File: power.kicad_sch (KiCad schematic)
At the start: 53 parts, among them J25 Conn_01x02, U1 TLV75733PDBV, U2 TPS56A37, U6 TPS5430DDA, U7 TPS56A37

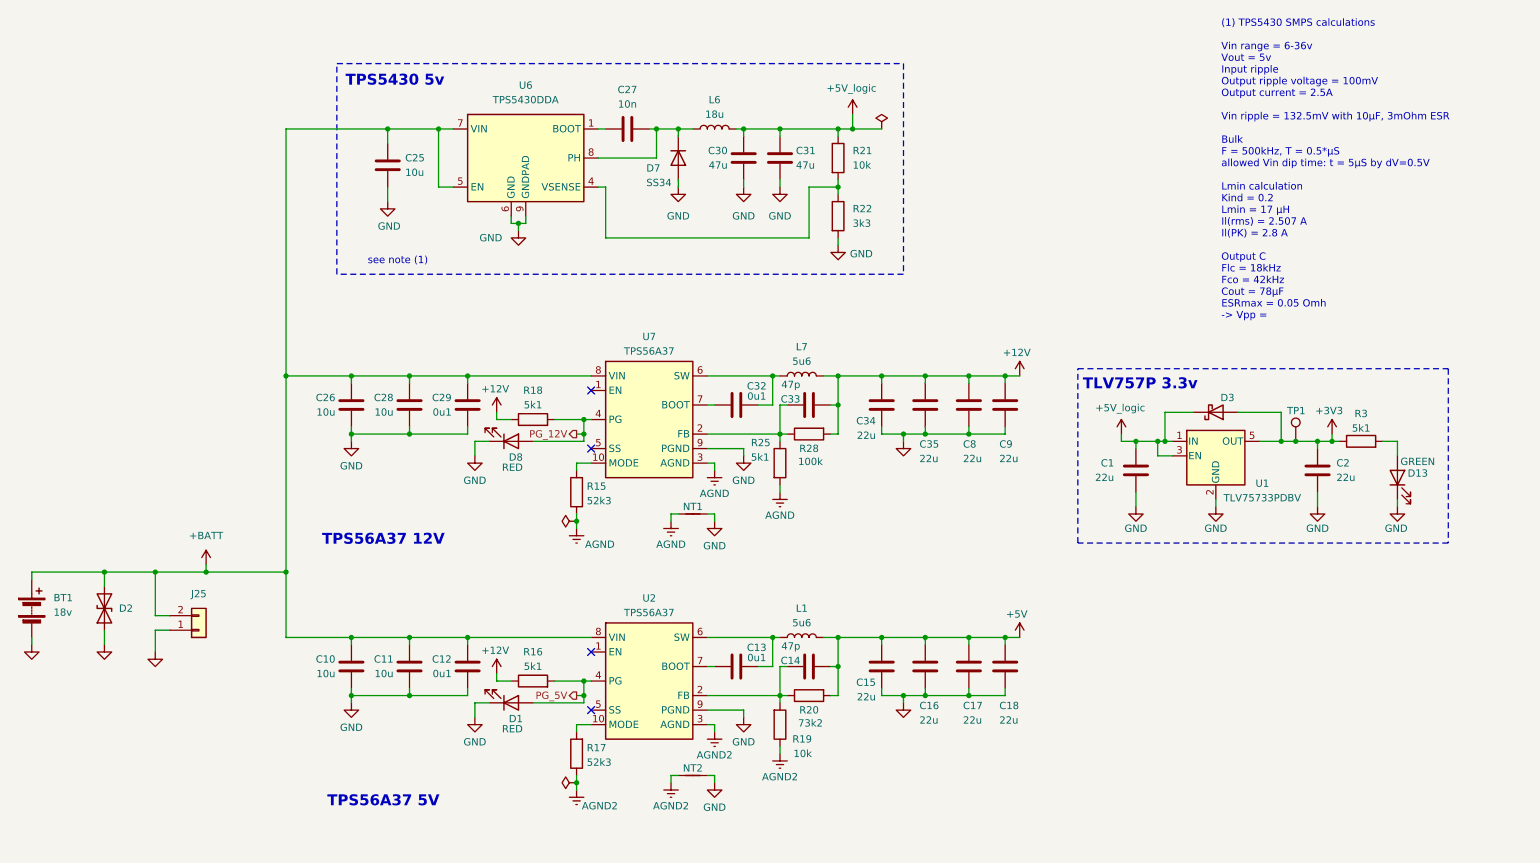
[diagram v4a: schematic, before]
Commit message: schem: remove logic 5V smps
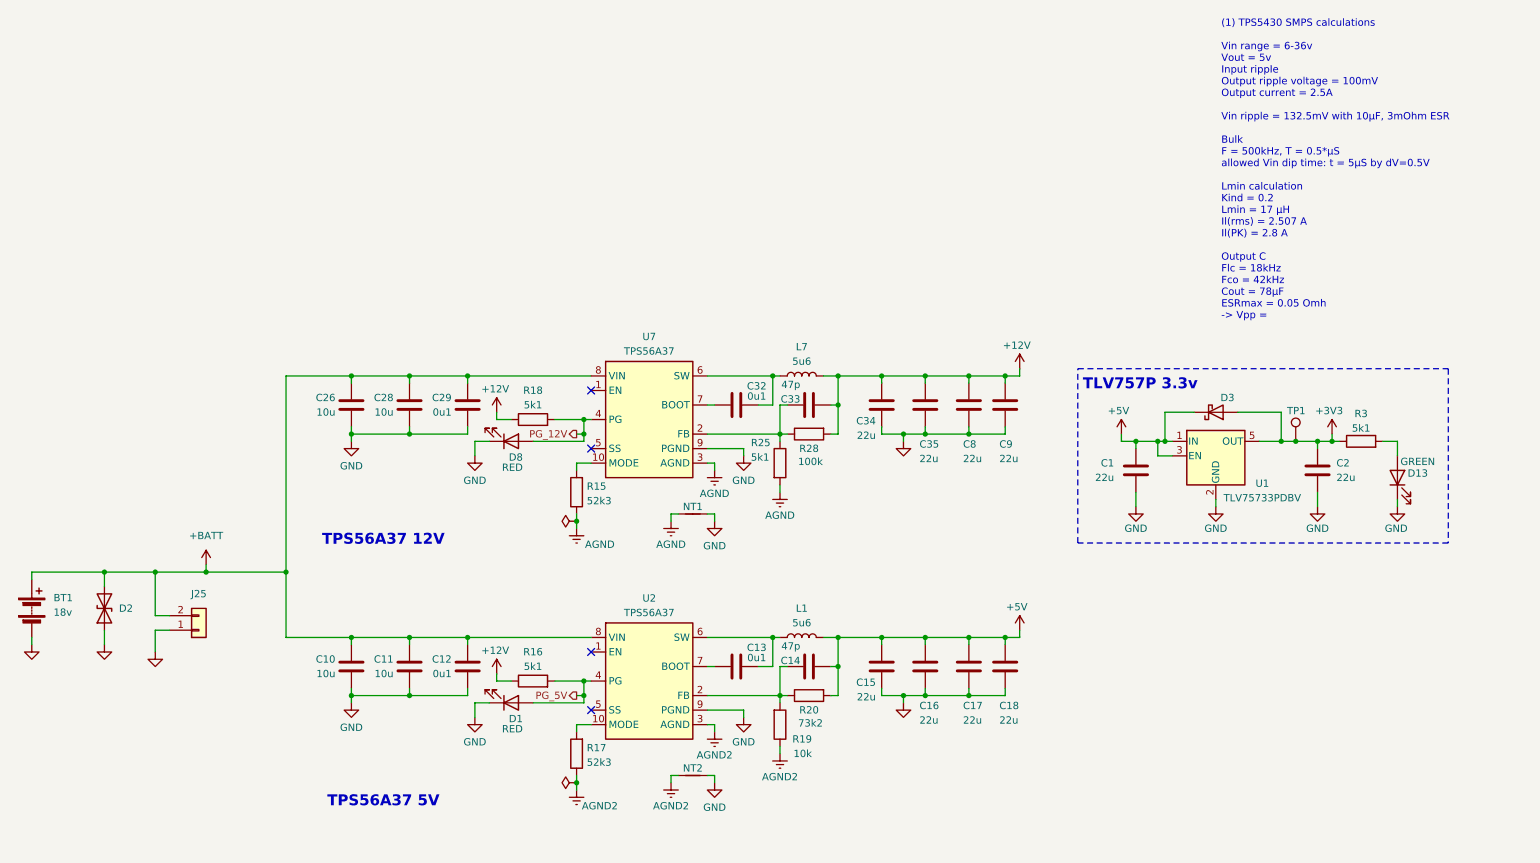
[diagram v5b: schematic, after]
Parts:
- removed C25: 10u, Capacitor_SMD:C_0805_2012Metric, symbol Device:C
- removed C27: 10n, Capacitor_SMD:C_0402_1005Metric, symbol Device:C
- removed C30, C31: 47u, Capacitor_SMD:C_1206_3216Metric, symbol Device:C
- removed D7: SS34, Diode_SMD:D_SMA, symbol Device:D
- removed L6: 18u, Inductor_SMD:L_Sunlord_SWRB1207S, symbol Device:L
- removed R21: 10k, Resistor_SMD:R_0402_1005Metric, symbol Device:R
- removed R22: 3k3, Resistor_SMD:R_0402_1005Metric, symbol Device:R
- removed U6: TPS5430DDA, Package_SO:TI_SO-PowerPAD-8_ThermalVias, symbol Regulator_Switching:TPS5430DDA
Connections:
- net +5V_logic is gone; now on net +5V: C1.2, D3.1 (K), U1.1 (IN), U1.3 (EN)
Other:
- note removed: "TPS5430 5v"
- note removed: "see note (1)"

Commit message: schem: add disable jumper to efuses
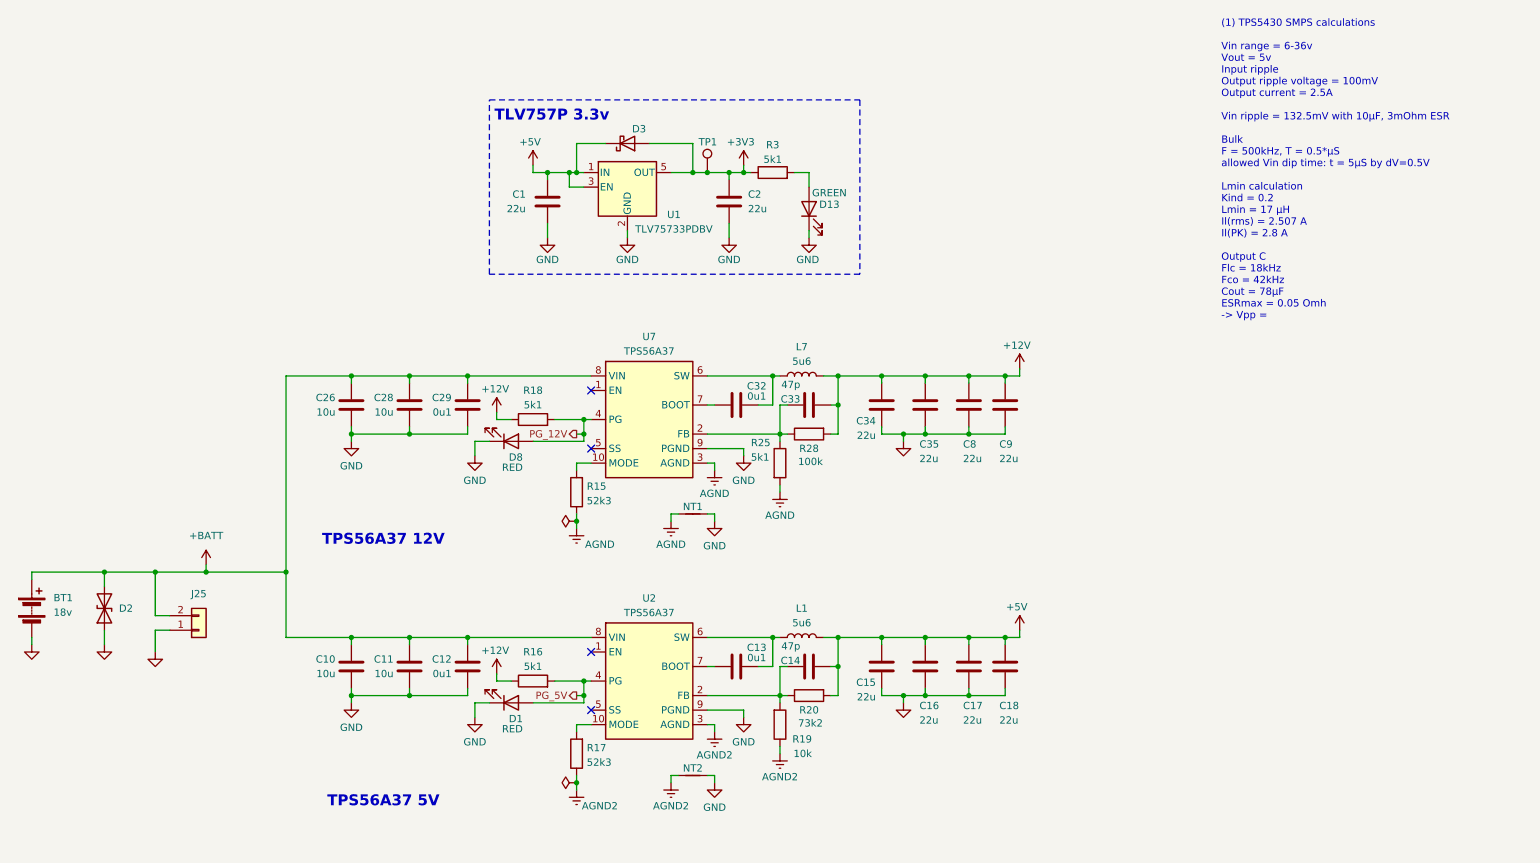
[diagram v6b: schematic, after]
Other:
- moved on the sheet: C1, C2, D13, D3, R3, TP1, U1

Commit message: schem: change aux batt power connector
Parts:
- J25: footprint Connector_JST:JST_XH_B2B-XH-A_1x02_P2.50mm_Vertical -> TerminalBlock_Phoenix:TerminalBlock_Phoenix_MKDS-1,5-2-5.08_1x02_P5.08mm_Horizontal
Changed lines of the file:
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@@
 			)
 		)
-		(property "Footprint" "Connector_JST:JST_XH_B2B-XH-A_1x02_P2.50mm_Vertical"
+		(property "Footprint" "TerminalBlock_Phoenix:TerminalBlock_Phoenix_MKDS-1,5-2-5.08_1x02_P5.08mm_Horizontal"
 			(at 55.88 121.92 0)
 			(effects

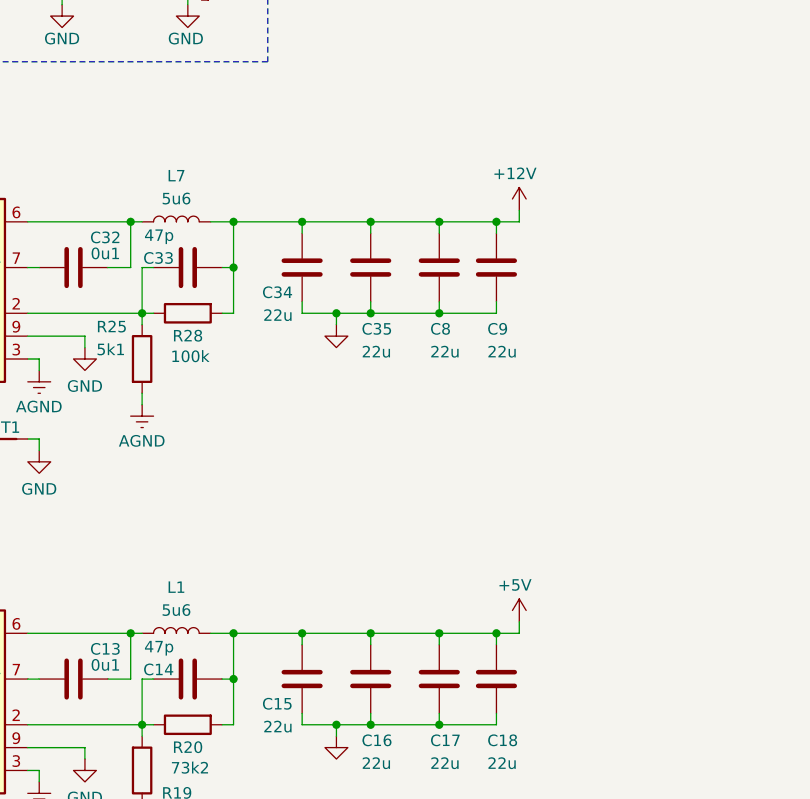
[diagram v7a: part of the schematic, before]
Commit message: schem: add test points
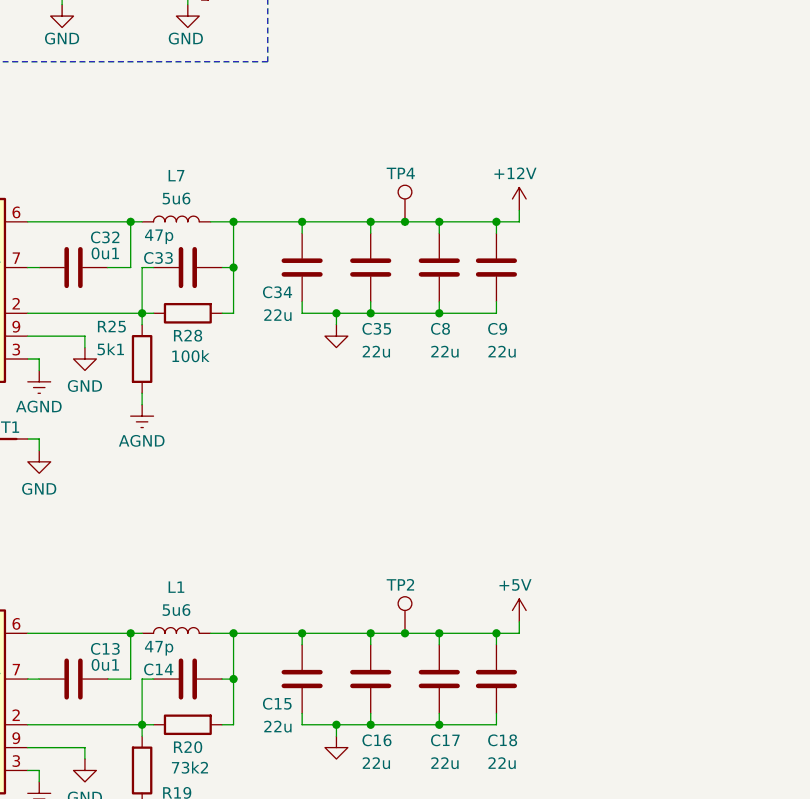
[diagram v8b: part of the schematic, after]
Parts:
- added TP2, TP4: TestPoint, TestPoint:TestPoint_Pad_D2.0mm, symbol Connector:TestPoint
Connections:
- net +12V: now also TP4.1
- net +5V: now also TP2.1
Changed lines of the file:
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@@
 	)
 	(junction
+		(at 186.69 123.19)
+		(diameter 0)
+		(color 0 0 0 0)
+	)
+	(junction
 		(at 167.64 77.47)
 		(diameter 0)
@@
 	)
 	(junction
+		(at 186.69 77.47)
+		(diameter 0)
+		(color 0 0 0 0)
+	)
+	(junction
 		(at 82.55 77.47)
 		(diameter 0)
@@
 	(wire
 		(pts
-			(xy 182.88 123.19) (xy 190.5 123.19)
+			(xy 182.88 123.19) (xy 186.69 123.19)
 		)
 		(stroke
@@
 	(wire
 		(pts
-			(xy 182.88 77.47) (xy 190.5 77.47)
+			(xy 182.88 77.47) (xy 186.69 77.47)
 		)
 		(stroke
@@
 	(wire
 		(pts
+			(xy 186.69 123.19) (xy 190.5 123.19)
+		)
+		(stroke
+			(width 0)
+			(type default)
+		)
+	)
+	(wire
+		(pts
 			(xy 138.43 101.6) (xy 139.7 101.6)
 		)
@@
 	(wire
 		(pts
+			(xy 186.69 77.47) (xy 190.5 77.47)
+		)
+		(stroke
+			(width 0)
+			(type default)
+		)
+	)
+	(wire
+		(pts
 			(xy 121.92 149.86) (xy 121.92 148.59)
 		)
@@
 	)
 	(symbol
+		(lib_id "Connector:TestPoint")
+		(at 186.69 77.47 0)
+		(unit 1)
+		(exclude_from_sim no)
+		(in_bom no)
+		(on_board yes)
+		(dnp no)
+		(property "Reference" "TP4"
+			(at 184.658 72.136 0)
+			(effects
+				(font
+					(size 1.27 1.27)
+				)
+				(justify left)
+			)
+		)
+		(property "Value" "TestPoint"
+			(at 189.23 75.4379 0)
+			(effects
+				(font
+					(size 1.27 1.27)
+				)
+				(justify left)
+				(hide yes)
+			)
+		)
+		(property "Footprint" "TestPoint:TestPoint_Pad_D2.0mm"
+			(at 191.77 77.47 0)
+			(effects
+				(font
+					(size 1.27 1.27)
+				)
+				(hide yes)
+			)
+		)
+		(property "Datasheet" "~"
+			(at 191.77 77.47 0)
+			(effects
+				(font
+					(size 1.27 1.27)
+				)
+				(hide yes)
+			)
+		)
+		(property "Description" "test point"
+			(at 186.69 77.47 0)
+			(effects
+				(font
+					(size 1.27 1.27)
+				)
+				(hide yes)
+			)
+		)
+		(pin "1"
+		)
+		(instances
+			(project "valrob-carte-alim-cdf-1"
+				(path "/8d7b287d-627f-46aa-8c27-0b5ed29ab4a2/0cc01053-a223-4e8e-b0aa-a1ec618db290"
+					(reference "TP4")
+					(unit 1)
+				)
+			)
+		)
+	)
+	(symbol
 		(lib_id "Device:C")
 		(at 102.87 128.27 0)
@@
 					(unit 1)
 				)
+			)
+		)
+	)
+	(symbol
+		(lib_id "Connector:TestPoint")
+		(at 186.69 123.19 0)
+		(unit 1)
+		(exclude_from_sim no)
+		(in_bom no)
+		(on_board yes)
+		(dnp no)
+		(property "Reference" "TP2"
+			(at 184.658 117.856 0)
+			(effects
+				(font
+					(size 1.27 1.27)
+				)
+				(justify left)
+			)
+		)
+		(property "Value" "TestPoint"
+			(at 189.23 121.1579 0)
+			(effects
+				(font
+					(size 1.27 1.27)
+				)
+				(justify left)
+				(hide yes)
+			)
+		)
+		(property "Footprint" "TestPoint:TestPoint_Pad_D2.0mm"
+			(at 191.77 123.19 0)
+			(effects
+				(font
+					(size 1.27 1.27)
+				)
+				(hide yes)
+			)
+		)
+		(property "Datasheet" "~"
+			(at 191.77 123.19 0)
+			(effects
+				(font
+					(size 1.27 1.27)
+				)
+				(hide yes)
+			)
+		)
+		(property "Description" "test point"
+			(at 186.69 123.19 0)
+			(effects
+				(font
+					(size 1.27 1.27)
+				)
+				(hide yes)
+			)
+		)
+		(pin "1"
+		)
+		(instances
+			(project "valrob-carte-alim-cdf-1"
+				(path "/8d7b287d-627f-46aa-8c27-0b5ed29ab4a2/0cc01053-a223-4e8e-b0aa-a1ec618db290"
+					(reference "TP2")
+					(unit 1)
+				)
